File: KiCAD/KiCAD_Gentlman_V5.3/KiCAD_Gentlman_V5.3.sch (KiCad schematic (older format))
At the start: 1 part, among them U1 STM32G070RBT6

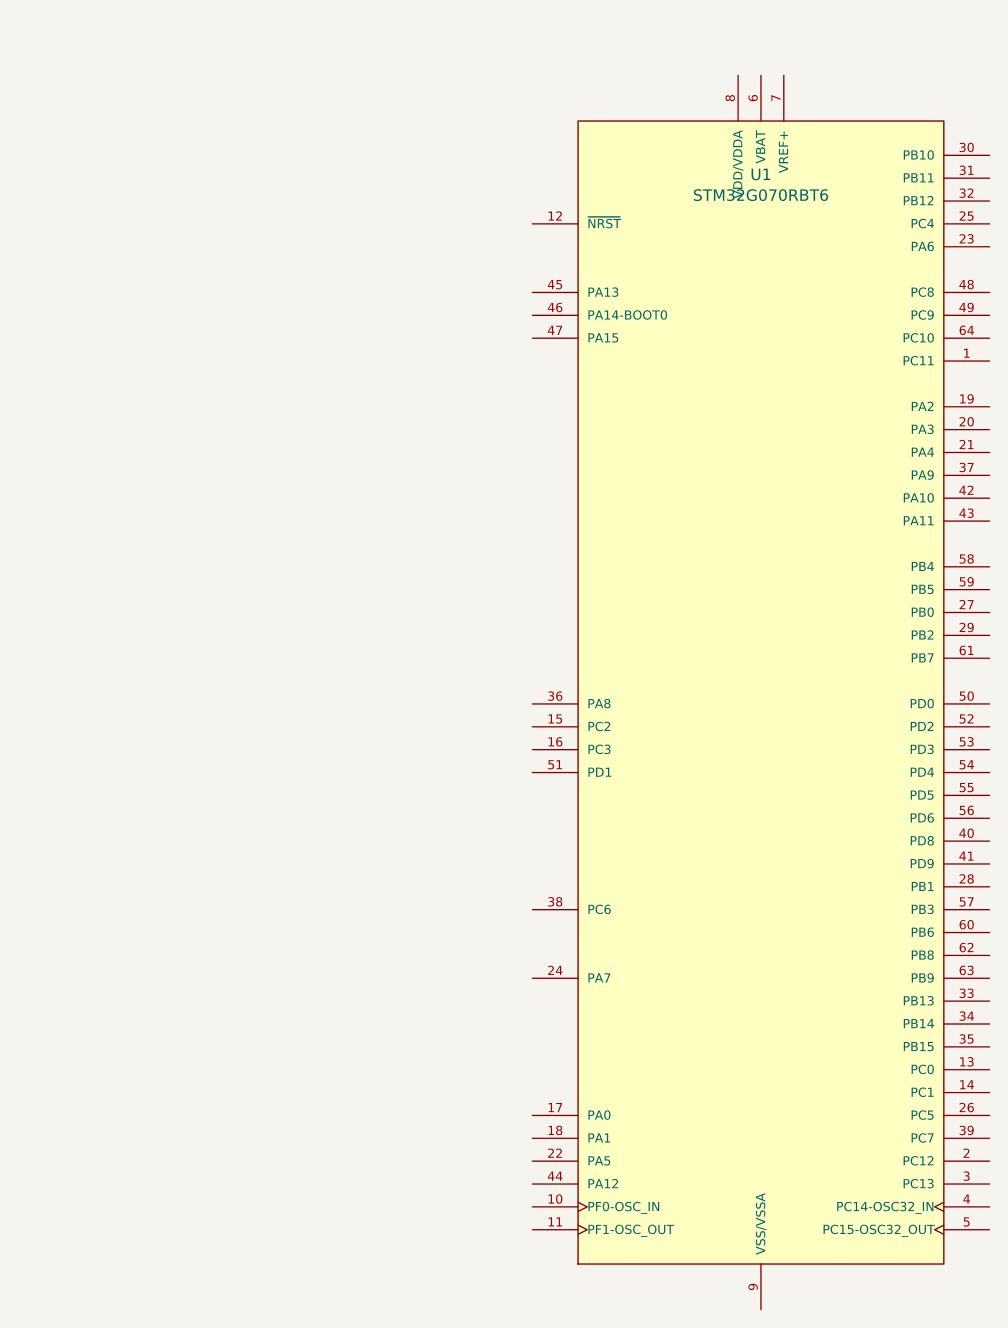
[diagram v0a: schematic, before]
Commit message: KSG : KICAD 라이브러리 대량 업데이트 및 회로도 제작 연습
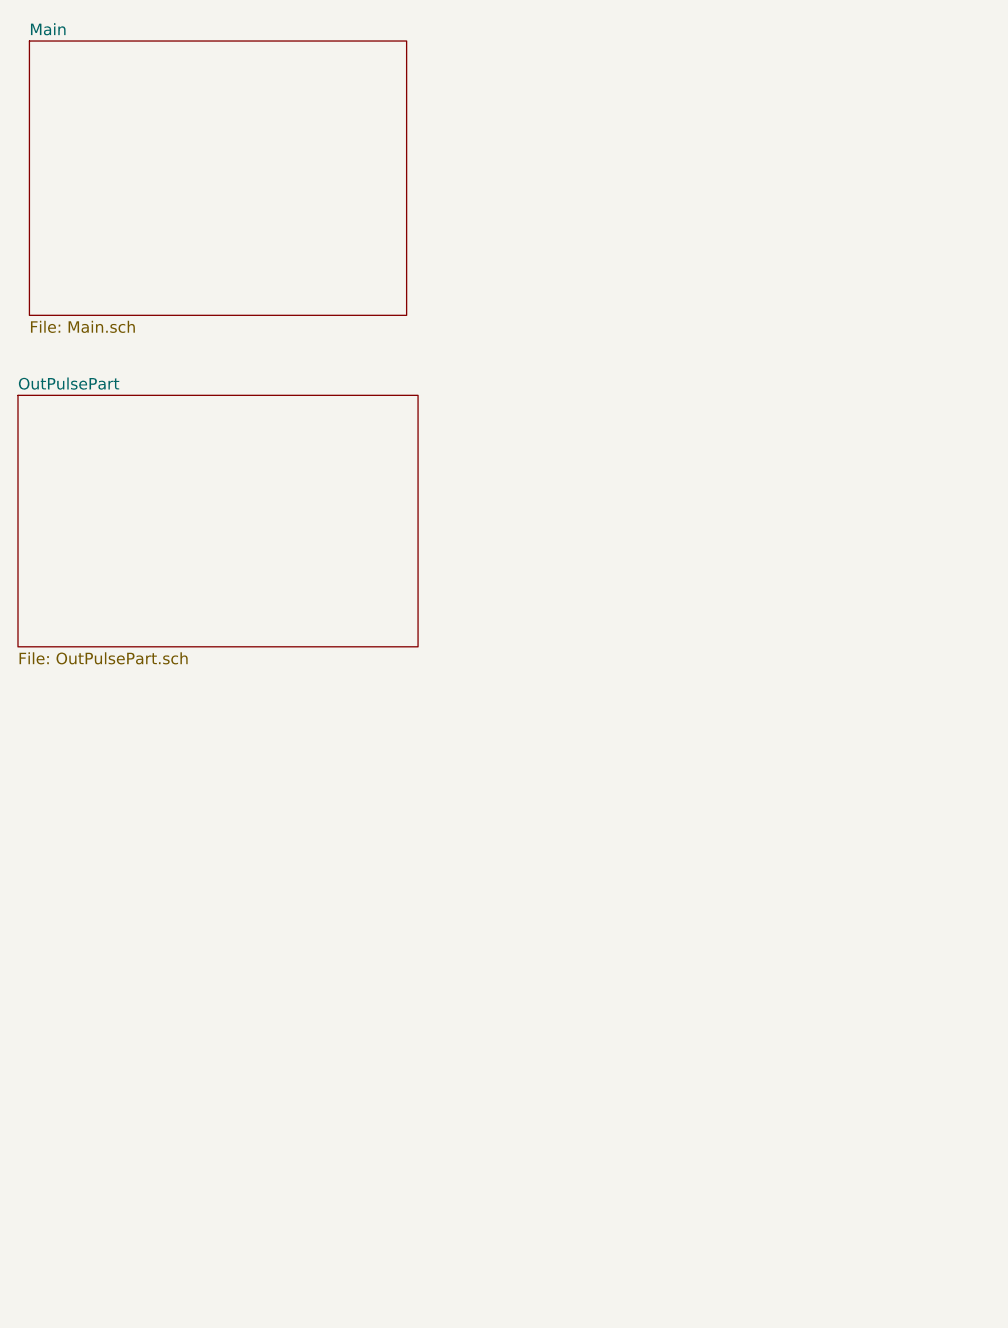
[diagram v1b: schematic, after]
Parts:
- removed U1: STM32G070RBT6, STM32G070RBT6:QFP50P1200X1200X160-64N, symbol STM32G070RBT6:STM32G070RBT6
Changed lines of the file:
@@
 EELAYER 30 0
 EELAYER END
-$Descr A4 11693 8268
+$Descr A3 16535 11693
 encoding utf-8
-Sheet 1 1
-Title ""
-Date ""
-Rev ""
-Comp ""
+Sheet 1 3
+Title "GentlemanV5.3"
+Date "2021-10-19"
+Rev "0.1"
+Comp "Psyche Co., Ltd"
 Comment1 ""
 Comment2 ""
@@
 Comment4 ""
 $EndDescr
-$Comp
-L STM32G070RBT6:STM32G070RBT6 U1
-U 1 1 616D88F7
-P 4050 3750
-F 0 "U1" H 4050 6015 50  0000 C CNN
-F 1 "STM32G070RBT6" H 4050 5924 50  0000 C CNN
-F 2 "STM32G070RBT6:QFP50P1200X1200X160-64N" H 4050 3750 50  0001 L BNN
-F 3 "" H 4050 3750 50  0001 L BNN
-F 4 "10.0" H 4050 3750 50  0001 L BNN "E1_MIN"
-F 5 "12.0" H 4050 3750 50  0001 L BNN "E_MAX"
-F 6 "0.6" H 4050 3750 50  0001 L BNN "L_NOM"
-F 7 "0.5" H 4050 3750 50  0001 L BNN "ENOM"
-F 8 "" H 4050 3750 50  0001 L BNN "JEDEC"
-F 9 "1.6mm" H 4050 3750 50  0001 L BNN "MAXIMUM_PACKAGE_HEIGHT"
-F 10 "12.0" H 4050 3750 50  0001 L BNN "E_MIN"
-F 11 "" H 4050 3750 50  0001 L BNN "BALL_ROWS"
-F 12 "" H 4050 3750 50  0001 L BNN "VACANCIES"
-F 13 "1.6" H 4050 3750 50  0001 L BNN "A_MAX"
-F 14 "" H 4050 3750 50  0001 L BNN "PACKAGE_TYPE"
-F 15 "0.17" H 4050 3750 50  0001 L BNN "B_MIN"
-F 16 "0.27" H 4050 3750 50  0001 L BNN "B_MAX"
-F 17 "" H 4050 3750 50  0001 L BNN "SNAPEDA_PACKAGE_ID"
-F 18 "0.22" H 4050 3750 50  0001 L BNN "B_NOM"
-F 19 "IPC 7351B" H 4050 3750 50  0001 L BNN "STANDARD"
-F 20 "12.0" H 4050 3750 50  0001 L BNN "E_NOM"
-F 21 "" H 4050 3750 50  0001 L BNN "BALL_COLUMNS"
-F 22 "10.0" H 4050 3750 50  0001 L BNN "D1_MIN"
-F 23 "1" H 4050 3750 50  0001 L BNN "PARTREV"
-F 24 "" H 4050 3750 50  0001 L BNN "BODY_DIAMETER"
-F 25 "" H 4050 3750 50  0001 L BNN "PINS"
-F 26 "10.0" H 4050 3750 50  0001 L BNN "E1_MAX"
-F 27 "0.0" H 4050 3750 50  0001 L BNN "E2_NOM"
-F 28 "10.0" H 4050 3750 50  0001 L BNN "E1_NOM"
-F 29 "12.0" H 4050 3750 50  0001 L BNN "D_NOM"
-F 30 "" H 4050 3750 50  0001 L BNN "IPC"
-F 31 "0.15" H 4050 3750 50  0001 L BNN "A1_MIN"
-F 32 "10.0" H 4050 3750 50  0001 L BNN "D1_MAX"
-F 33 "" H 4050 3750 50  0001 L BNN "PIN_COLUMNS"
-F 34 "" H 4050 3750 50  0001 L BNN "EMAX"
-F 35 "12.0" H 4050 3750 50  0001 L BNN "D_MIN"
-F 36 "0.75" H 4050 3750 50  0001 L BNN "L_MAX"
-F 37 "10.0" H 4050 3750 50  0001 L BNN "D1_NOM"
-F 38 "0.45" H 4050 3750 50  0001 L BNN "L_MIN"
-F 39 "" H 4050 3750 50  0001 L BNN "THERMAL_PAD"
-F 40 "16.0" H 4050 3750 50  0001 L BNN "PIN_COUNT_D"
-F 41 "16.0" H 4050 3750 50  0001 L BNN "PIN_COUNT_E"
-F 42 "ST" H 4050 3750 50  0001 L BNN "MANUFACTURER"
-F 43 "" H 4050 3750 50  0001 L BNN "EMIN"
-F 44 "12.0" H 4050 3750 50  0001 L BNN "D_MAX"
-F 45 "0.0" H 4050 3750 50  0001 L BNN "D2_NOM"
-	1    4050 3750
-	1    0    0    -1
-$EndComp
+$Sheet
+S 850  900  1650 1200
+U 616E62D0
+F0 "Main" 50
+F1 "Main.sch" 50
+$EndSheet
+$Sheet
+S 800  2450 1750 1100
+U 616E6A47
+F0 "OutPulsePart" 50
+F1 "OutPulsePart.sch" 50
+$EndSheet
 $EndSCHEMATC

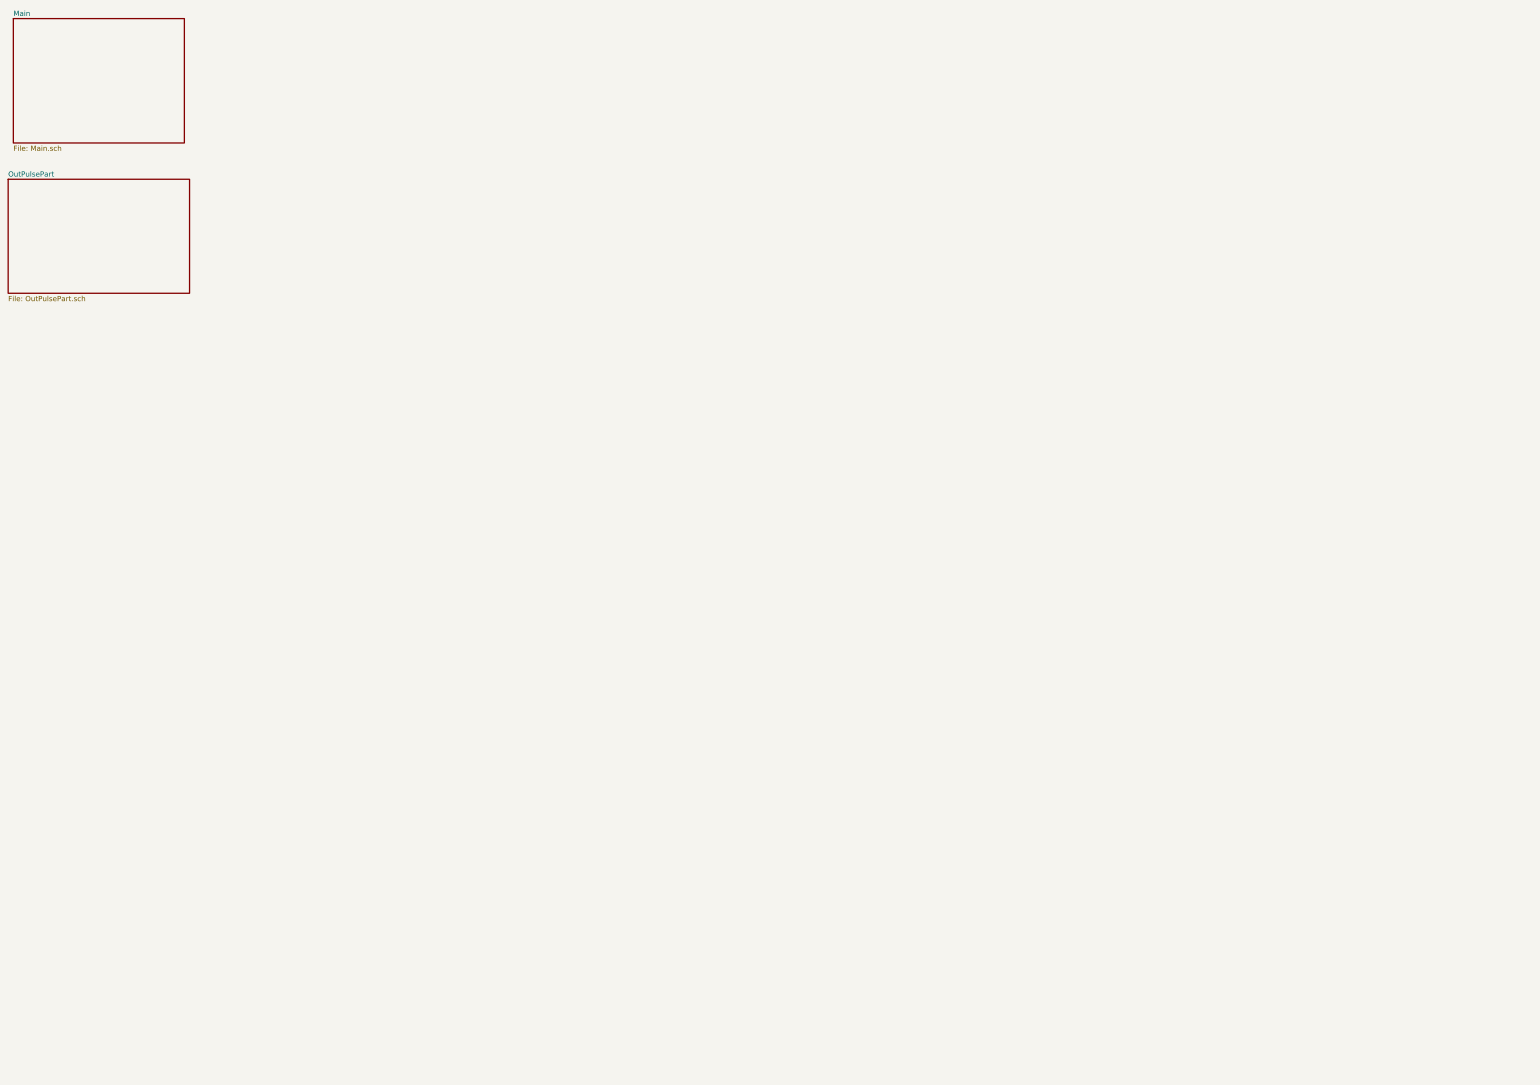
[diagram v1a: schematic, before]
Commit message: KSG : V5.3 회로도 초본 완성(검토 필요) 일부 부품 데이터시트 추가
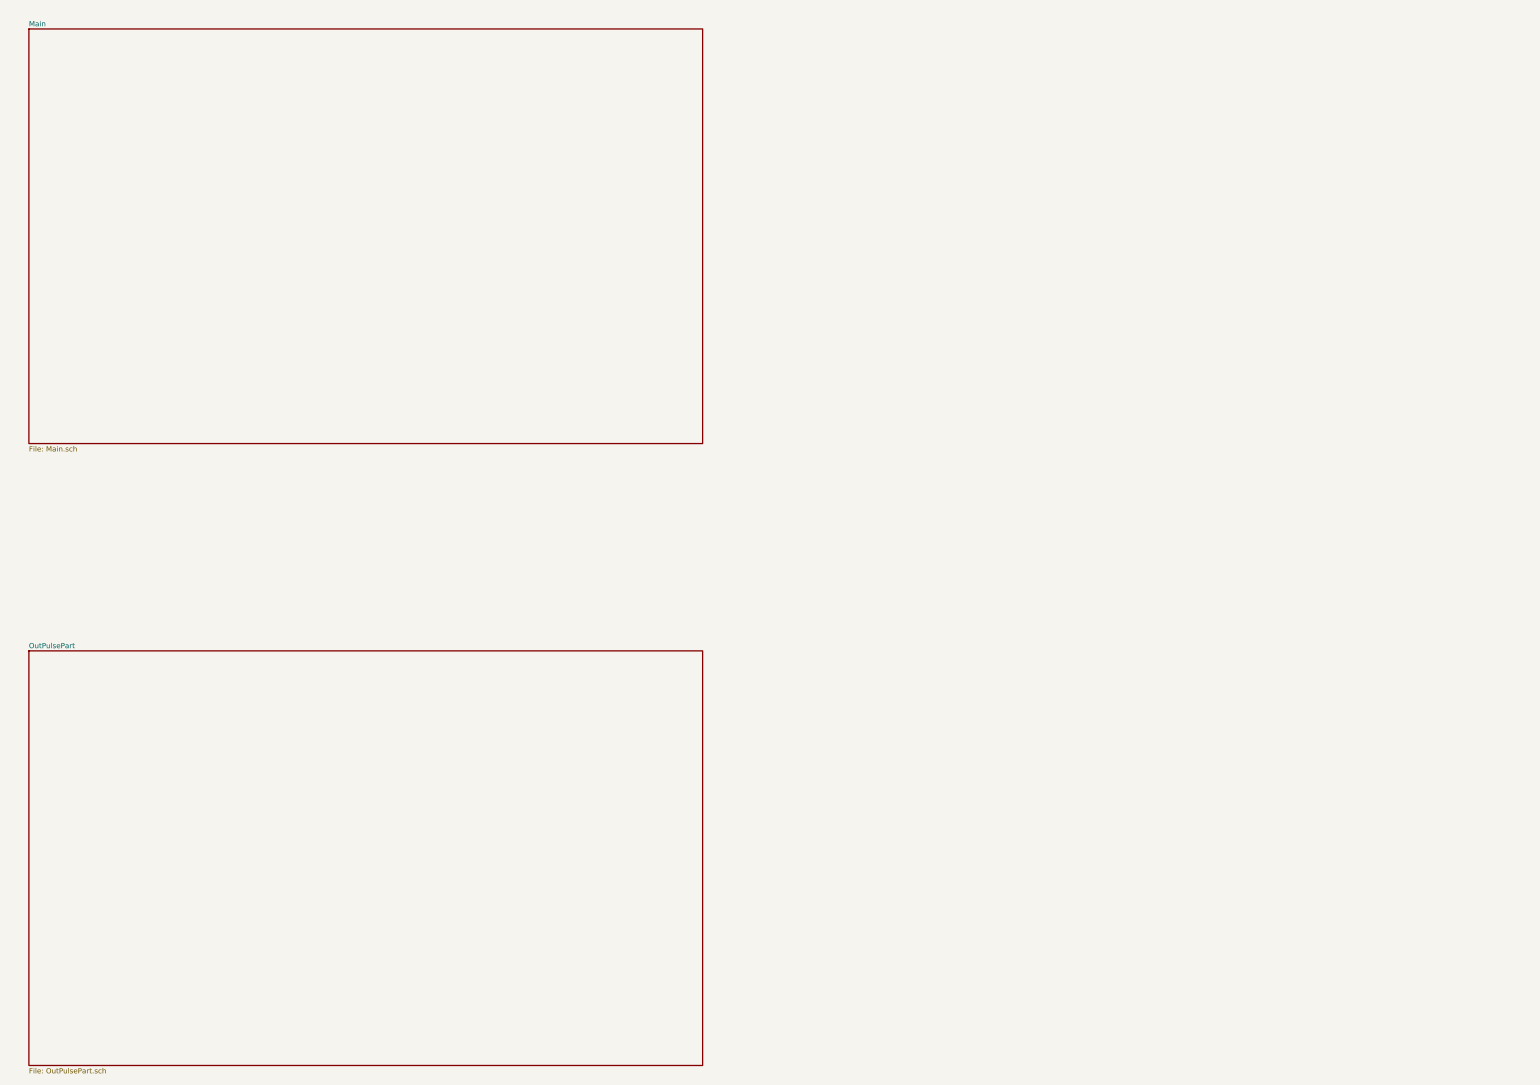
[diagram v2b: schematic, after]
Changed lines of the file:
@@
 $EndDescr
 $Sheet
-S 850  900  1650 1200
+S 1000 1000 6500 4000
 U 616E62D0
 F0 "Main" 50
@@
 $EndSheet
 $Sheet
-S 800  2450 1750 1100
+S 1000 7000 6500 4000
 U 616E6A47
 F0 "OutPulsePart" 50

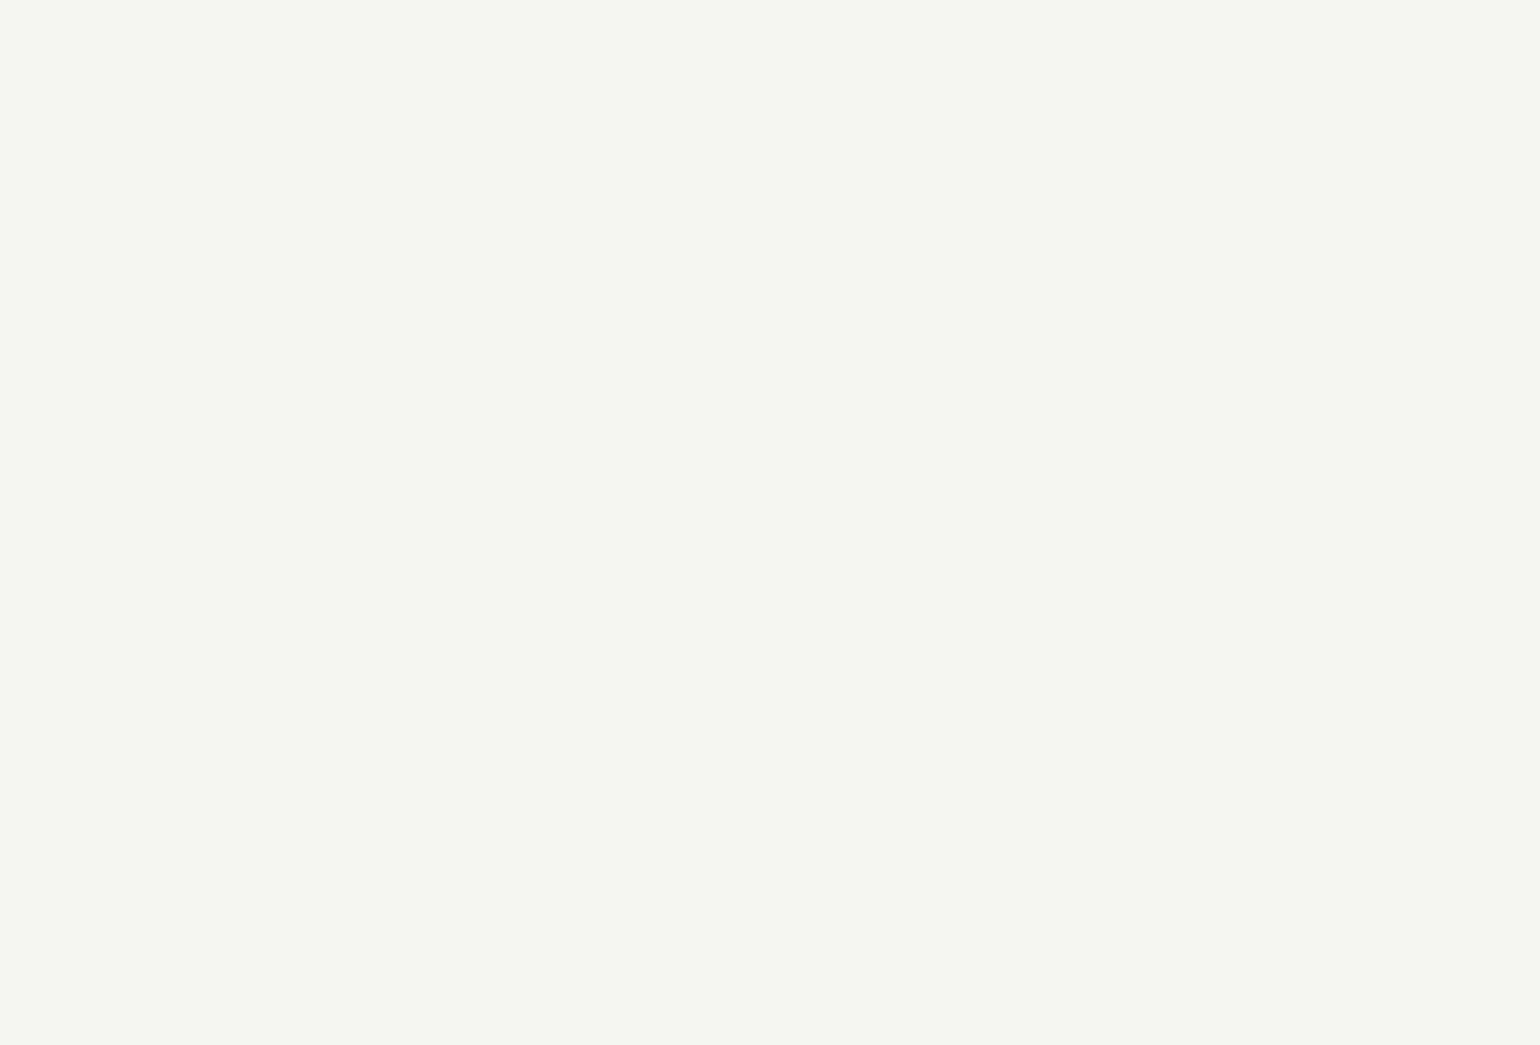
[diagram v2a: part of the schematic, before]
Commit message: KSG : 블루투스 회로도 작성 완료 (풋프린트 및 데이터시트 업데이트 완료)
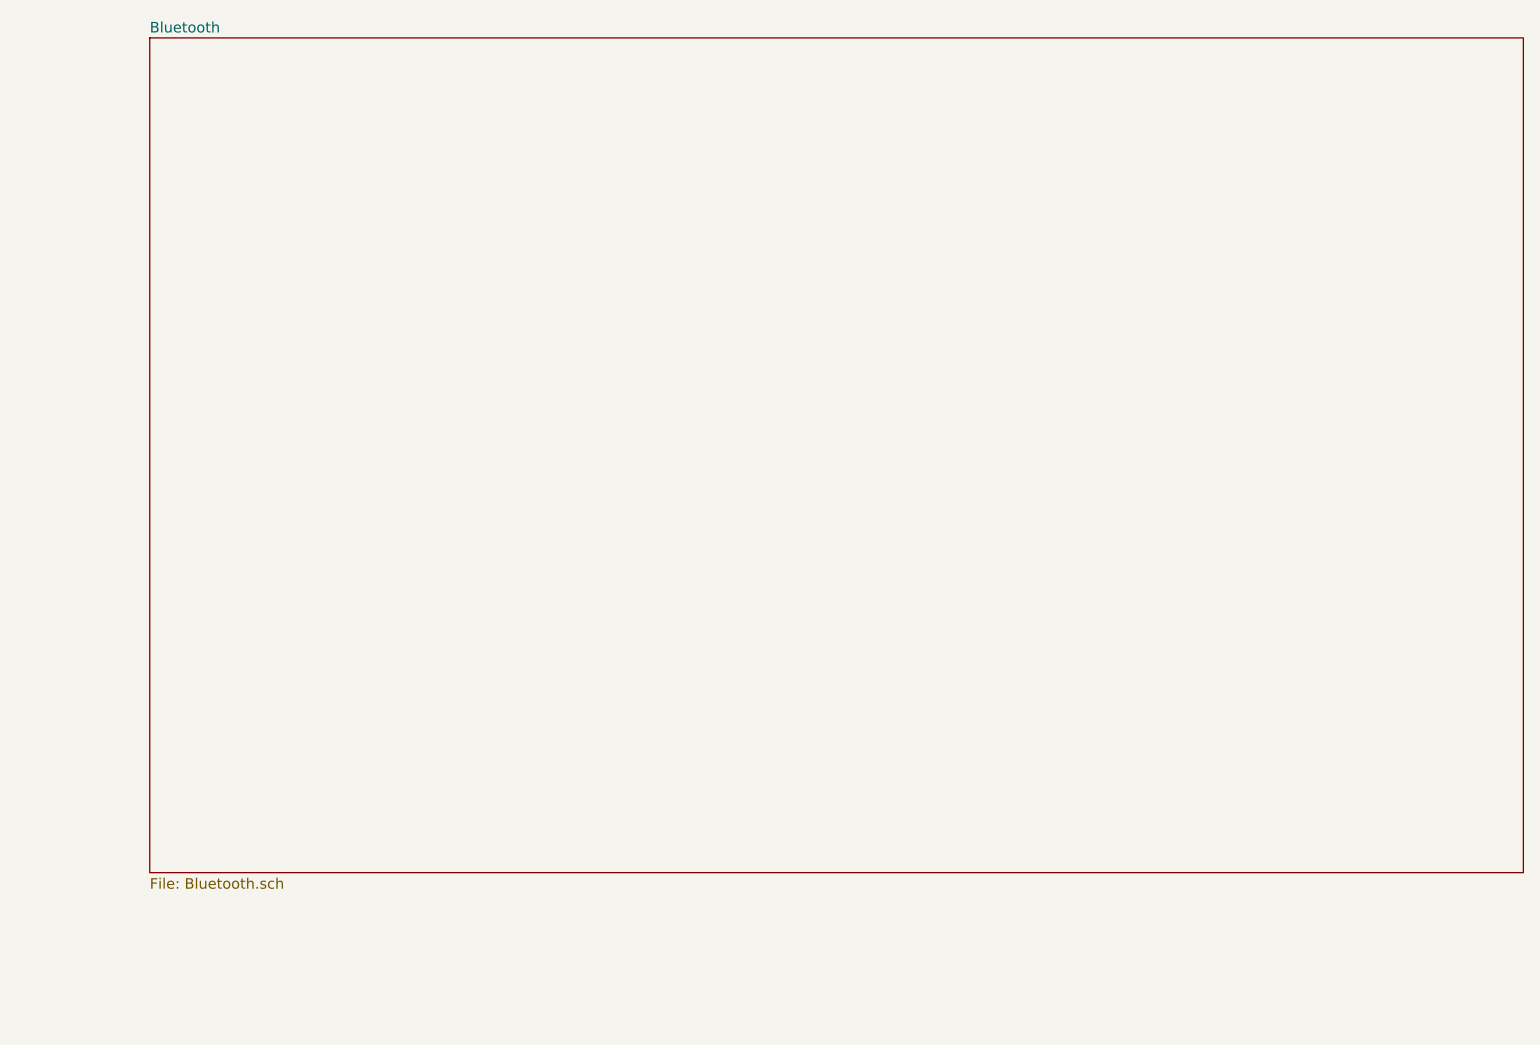
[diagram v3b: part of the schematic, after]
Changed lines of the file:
@@
 $Descr A3 16535 11693
 encoding utf-8
-Sheet 1 3
+Sheet 1 4
 Title "GentlemanV5.3"
 Date "2021-10-19"
@@
 F1 "OutPulsePart.sch" 50
 $EndSheet
+$Sheet
+S 9000 1000 6500 3950
+U 61979BEC
+F0 "Bluetooth" 50
+F1 "Bluetooth.sch" 50
+$EndSheet
 $EndSCHEMATC
